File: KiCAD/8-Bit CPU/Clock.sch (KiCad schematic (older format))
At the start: 21 parts, among them SW7 MODE, SW8 CLK, U49 74HC14, U50 74HC1G08, U51 74HC1G08, U52 74HC1G32

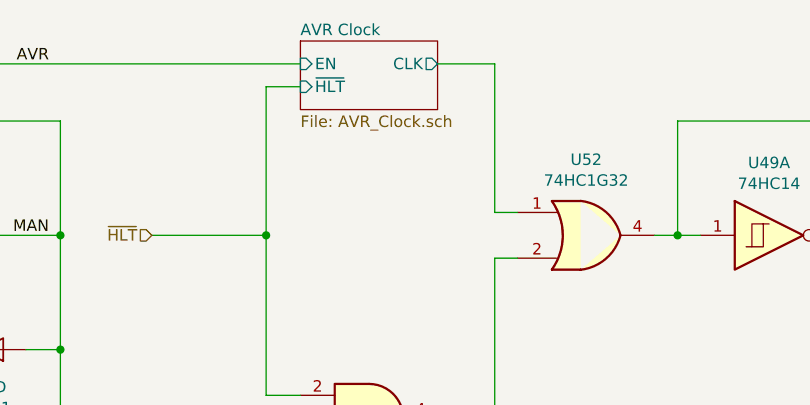
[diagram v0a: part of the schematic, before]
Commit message: KiCAD cleanup - Revision A
Revision A Known Issues:
 * ATTiny45 has incorrect footprint
 * Flags register is redundant (The ATMega16's output port is a register)
 * Power jack pinout is wrong (12V shorted to ground)
 * Step counter reset logic is wrong (Active high signalling, Active low input)
 * ALU output indicator not connected
 * HLT indicator missing
 * EEPROMs can't be page written due to addressing setup (minor annoyance)
 * Flags Logic uses NAND gates instead of AND (fixed on the board I built)
 * Programmer needs to be able to toggle EEPROM outputs and Addressing Devices
    with different signals to enable reading.
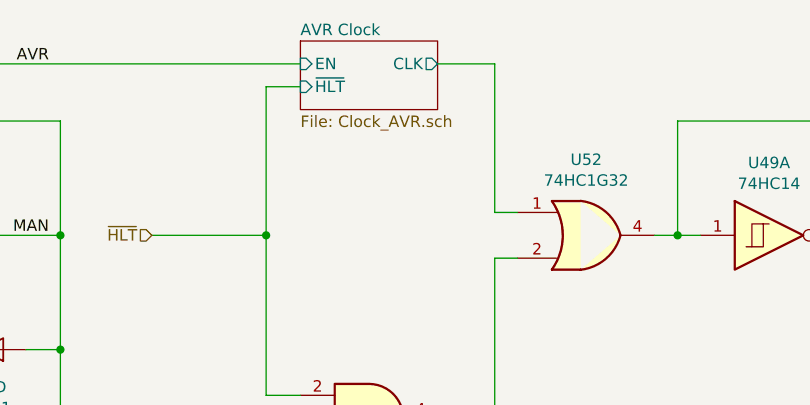
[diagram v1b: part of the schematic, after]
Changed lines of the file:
@@
 $Descr A4 11693 8268
 encoding utf-8
-Sheet 29 30
+Sheet 29 29
 Title ""
 Date ""
@@
 U 5D6FC11A
 F0 "AVR Clock" 50
-F1 "AVR_Clock.sch" 50
+F1 "Clock_AVR.sch" 50
 F2 "~HLT" I L 5150 1350 50
 F3 "EN" I L 5150 1250 50

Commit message: KiCAD files update & Gerbers
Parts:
- added D107: RED, LED_SMD:LED_0805_2012Metric, symbol Device:LED
- added R47: 1k, Resistor_SMD:R_0805_2012Metric, symbol Device:R
- renumbered C59 to C58, C58 to C59, D102 to D104, D100 to D105, D101 to D106, R47 to R41, R49 to R42, R46 to R43, R48 to R44, R44 to R45, R45 to R46, U52 to U50, U50 to U52
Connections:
- net VCC: now also R47.2
- net ~HLT: now also D107.1 (K)
- new net: D107.2 (A), R47.1
